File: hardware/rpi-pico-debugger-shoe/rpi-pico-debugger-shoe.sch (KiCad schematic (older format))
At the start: 2 parts, among them U1 RP2040, U2 AP2112K-3.3TRG1

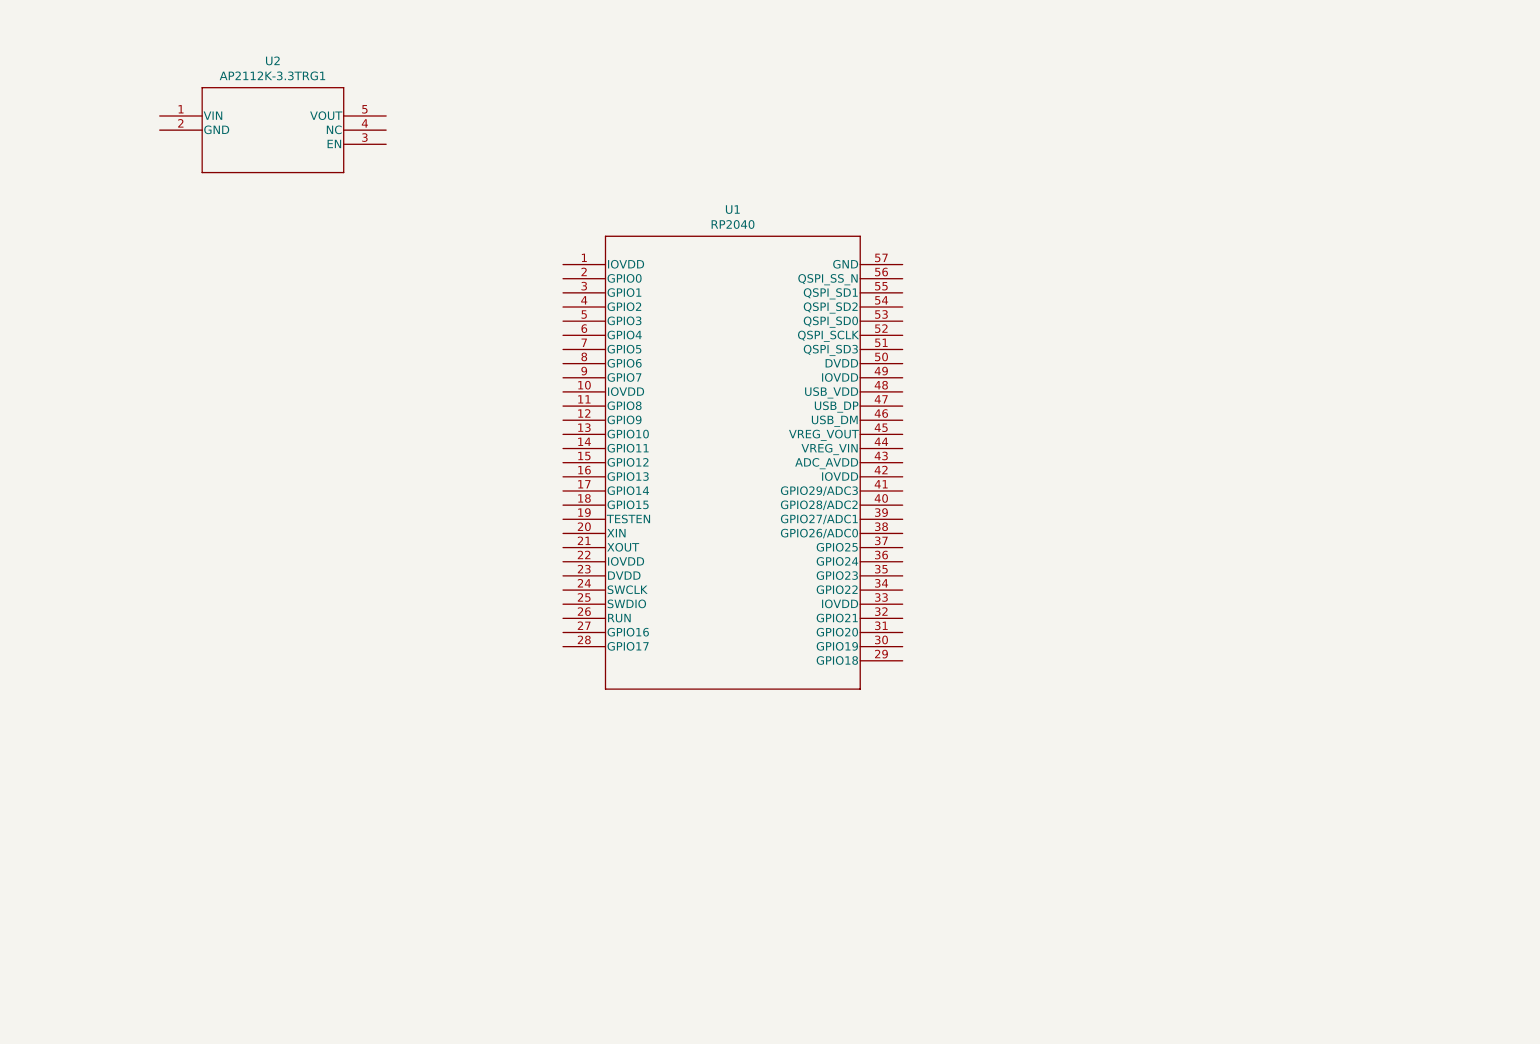
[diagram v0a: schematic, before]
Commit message: Finished schematic and BOM for v01
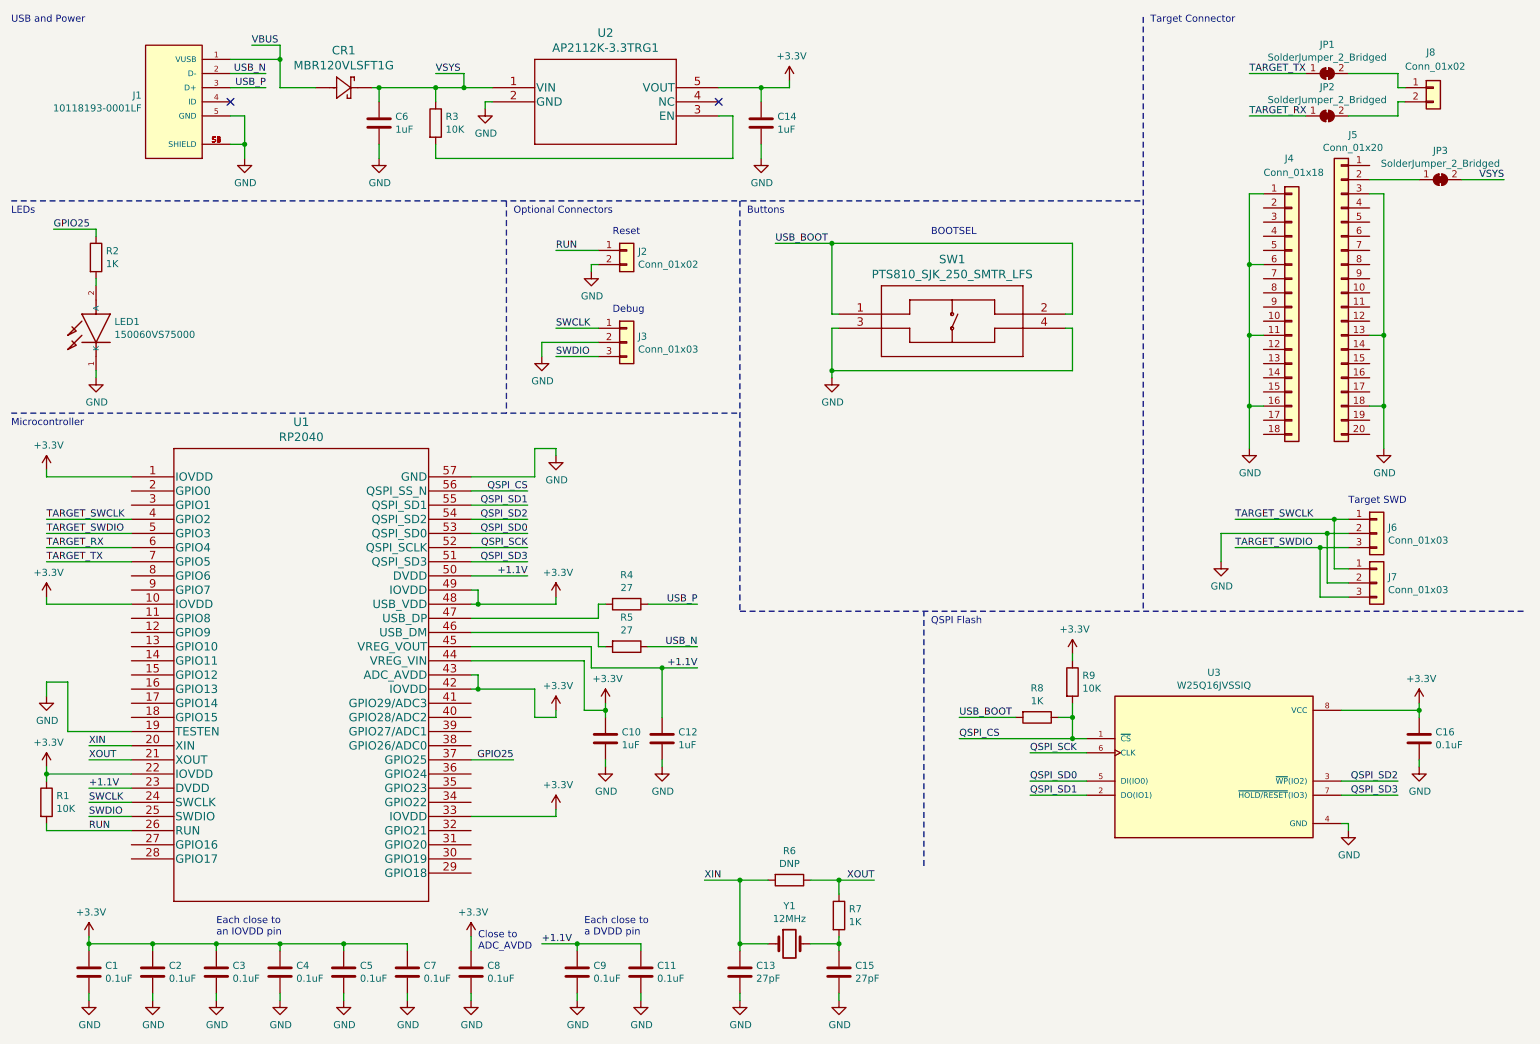
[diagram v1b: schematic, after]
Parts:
- added C1, C11, C16, C2, C3, C4, C5, C7, C8, C9: 0.1uF, Capacitor_SMD:C_0603_1608Metric_Pad1.08x0.95mm_HandSolder, symbol Device:C
- added C10, C12, C14, C6: 1uF, Capacitor_SMD:C_0603_1608Metric_Pad1.08x0.95mm_HandSolder, symbol Device:C
- added C13, C15: 27pF, Capacitor_SMD:C_0603_1608Metric_Pad1.08x0.95mm_HandSolder, symbol Device:C
- added CR1: MBR120VLSFT1G, mbr120vlsft1g:MBR120VLSFT1G, symbol 2021-05-12_00-49-18:MBR120VLSFT1G
- added J1: 10118193-0001LF, 10118193-0001LF:FCI_10118193-0001LF, symbol 10118193-0001LF:10118193-0001LF
- added J2, J8: Conn_01x02, Connector_PinHeader_2.54mm:PinHeader_1x02_P2.54mm_Vertical, symbol Connector_Generic:Conn_01x02
- added J3, J6, J7: Conn_01x03, Connector_PinHeader_2.54mm:PinHeader_1x03_P2.54mm_Vertical, symbol Connector_Generic:Conn_01x03
- added J4: Conn_01x18, Connector_PinHeader_2.54mm:PinHeader_1x18_P2.54mm_Vertical, symbol Connector_Generic:Conn_01x18
- added J5: Conn_01x20, Connector_PinHeader_2.54mm:PinHeader_1x20_P2.54mm_Vertical, symbol Connector_Generic:Conn_01x20
- added JP1, JP2, JP3: SolderJumper_2_Bridged, Jumper:SolderJumper-2_P1.3mm_Bridged_RoundedPad1.0x1.5mm, symbol Jumper:SolderJumper_2_Bridged
- added LED1: 150060VS75000, 150060VS75000:LEDC1608X80N, symbol 150060VS75000:150060VS75000
- added R1, R3, R9: 10K, Resistor_SMD:R_0603_1608Metric_Pad0.98x0.95mm_HandSolder, symbol Device:R
- added R2, R7, R8: 1K, Resistor_SMD:R_0603_1608Metric_Pad0.98x0.95mm_HandSolder, symbol Device:R
- added R4, R5: 27, Resistor_SMD:R_0603_1608Metric_Pad0.98x0.95mm_HandSolder, symbol Device:R
- added R6: DNP, Resistor_SMD:R_0603_1608Metric_Pad0.98x0.95mm_HandSolder, symbol Device:R
- added SW1: PTS810_SJK_250_SMTR_LFS, PTS810 SJK 250 SMTR LFS:PTS810 SJK 250 SMTR LFS, symbol 2021-05-12_02-12-02:PTS810_SJK_250_SMTR_LFS
- added U3: W25Q16JVSSIQ, W25Q16JVSSIQ:SOIC127P790X216-8N, symbol W25Q16JVSSIQ:W25Q16JVSSIQ
- added Y1: 12MHz, abls7m:ABLS7M2-16.000MHZ-D-2Y-T, symbol Device:Crystal
- U1: Digi-Key_PN (none) -> TBD
- U2: Digi-Key_PN (none) -> AP2112K-3.3TRG1DICT-ND
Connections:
- net +3V3: now reaches U1.1 (IOVDD)
- net +3V3: now also U1.10 (IOVDD), U1.22 (IOVDD), U1.33 (IOVDD), U1.42 (IOVDD), U1.43 (ADC_AVDD), U1.44 (VREG_VIN), U1.48 (USB_VDD), U1.49 (IOVDD), U2.5 (VOUT), C1.1, C10.1, C14.1, C16.1, C2.1, C3.1, C4.1, C5.1, C7.1, C8.1, R1.1, R9.1, U3.8 (VCC)
- net GND: now reaches U1.19 (TESTEN)
- net GND: now also U1.57 (GND), U2.2 (GND), C1.2, C10.2, C11.2, C12.2, C13.2, C14.2, C15.2, C16.2, C2.2, C3.2, C4.2, C5.2, C6.2, C7.2, C8.2, C9.2, J1.5 (GND), J1.S1 (SHIELD), J1.S2 (SHIELD), J1.S3 (SHIELD), J1.S4 (SHIELD), J1.S5 (SHIELD), J1.S6 (SHIELD), J2.2 (Pin_2), J3.2 (Pin_2), J4.1 (Pin_1), J4.11 (Pin_11), J4.16 (Pin_16), J4.6 (Pin_6), J5.13 (Pin_13), J5.18 (Pin_18), J5.3 (Pin_3), J6.2 (Pin_2), J7.2 (Pin_2), LED1.1 (K), SW1.3, SW1.4, U3.4 (GND)
- net XIN: now reaches U1.20 (XIN)
- net XIN: now also C13.1, R6.2, Y1.1
- net XOUT: now reaches U1.21 (XOUT)
- net XOUT: now also R6.1, R7.1
- net +1.1V: now reaches U1.23 (DVDD)
- net +1.1V: now also U1.45 (VREG_VOUT), U1.50 (DVDD), C11.1, C12.1, C9.1
- net SWCLK: now reaches U1.24 (SWCLK)
- net SWCLK: now also J3.1 (Pin_1)
- net SWDIO: now reaches U1.25 (SWDIO)
- net SWDIO: now also J3.3 (Pin_3)
- net RUN: now reaches U1.26 (RUN)
- net RUN: now also J2.1 (Pin_1), R1.2
- net GPIO25: now reaches U1.37 (GPIO25)
- net GPIO25: now also R2.1
- net TARGET_SWCLK: now reaches U1.4 (GPIO2)
- net TARGET_SWCLK: now also J6.1 (Pin_1), J7.1 (Pin_1)
- net at U1.46 (USB_DM): now also R5.2
- net at U1.47 (USB_DP): now also R4.2
- net TARGET_SWDIO: now reaches U1.5 (GPIO3)
- net TARGET_SWDIO: now also J6.3 (Pin_3), J7.3 (Pin_3)
- net QSPI_SD3: now reaches U1.51 (QSPI_SD3)
- net QSPI_SD3: now also U3.7 (~HOLD/RESET~(IO3))
- net QSPI_SCK: now reaches U1.52 (QSPI_SCLK)
- net QSPI_SCK: now also U3.6 (CLK)
- net QSPI_SD0: now reaches U1.53 (QSPI_SD0)
- net QSPI_SD0: now also U3.5 (DI(IO0))
- net QSPI_SD2: now reaches U1.54 (QSPI_SD2)
- net QSPI_SD2: now also U3.3 (~WP~(IO2))
- net QSPI_SD1: now reaches U1.55 (QSPI_SD1)
- net QSPI_SD1: now also U3.2 (DO(IO1))
- net QSPI_CS: now reaches U1.56 (QSPI_SS_N)
- net QSPI_CS: now also R8.1, R9.2, U3.1 (~CS)
- net TARGET_RX: now reaches U1.6 (GPIO4)
- net TARGET_RX: now also JP2.1 (A)
- net TARGET_TX: now reaches U1.7 (GPIO5)
- net TARGET_TX: now also JP1.1 (A)
- net VSYS: now reaches U2.1 (VIN)
- net VSYS: now also C6.1, CR1.1, JP3.2 (B), R3.1
- net at U2.3 (EN): now also R3.2
- new net: C15.1, R7.2, Y1.2
- new net: LED1.2 (A), R2.2
- new net: J5.2 (Pin_2), JP3.1 (A)
- new net: J8.1 (Pin_1), JP1.2 (B)
- new net: J8.2 (Pin_2), JP2.2 (B)
- new net USB_BOOT: R8.2, SW1.1, SW1.2
- new net USB_N: J1.2 (D-), R5.1
- new net USB_P: J1.3 (D+), R4.1
- new net VBUS: CR1.2, J1.1 (VUSB)
- no-connect marks 0 -> 2
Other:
- note added: "BOOTSEL"
- note added: "Buttons"
- note added: "Close to\nADC_AVDD"
- note added: "Debug"
- note added: "Each close to\na DVDD pin"
- note added: "Each close to\nan IOVDD pin"
- note added: "LEDs"
- note added: "Microcontroller"
- note added: "Optional Connectors"
- note added: "QSPI Flash"
- note added: "Reset"
- note added: "Target Connector"
- note added: "Target SWD"
- note added: "USB and Power"
- moved on the sheet: U1, U2

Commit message: Did done some layouts
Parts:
- added FID1, FID2: Fiducial, Fiducial:Fiducial_1mm_Mask2mm, symbol Mechanical:Fiducial
- added H1, H2, H3, H4: MountingHole, MountingHole:MountingHole_2.1mm, symbol Mechanical:MountingHole
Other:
- note added: "Mechanical"
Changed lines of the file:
@@
 Text Notes 7000 4800 0    50   ~ 0
 QSPI Flash
+$Comp
+L Mechanical:MountingHole H3
+U 1 1 609F6F52
+P 7800 1050
+F 0 "H3" H 7900 1096 50  0000 L CNN
+F 1 "MountingHole" H 7900 1005 50  0000 L CNN
+F 2 "MountingHole:MountingHole_2.1mm" H 7800 1050 50  0001 C CNN
+F 3 "~" H 7800 1050 50  0001 C CNN
+	1    7800 1050
+	1    0    0    -1
+$EndComp
+$Comp
+L Mechanical:MountingHole H4
+U 1 1 609F7AD6
+P 7800 1300
+F 0 "H4" H 7900 1346 50  0000 L CNN
+F 1 "MountingHole" H 7900 1255 50  0000 L CNN
+F 2 "MountingHole:MountingHole_2.1mm" H 7800 1300 50  0001 C CNN
+F 3 "~" H 7800 1300 50  0001 C CNN
+	1    7800 1300
+	1    0    0    -1
+$EndComp
+$Comp
+L Mechanical:MountingHole H2
+U 1 1 609F7D93
+P 7050 1300
+F 0 "H2" H 7150 1346 50  0000 L CNN
+F 1 "MountingHole" H 7150 1255 50  0000 L CNN
+F 2 "MountingHole:MountingHole_2.1mm" H 7050 1300 50  0001 C CNN
+F 3 "~" H 7050 1300 50  0001 C CNN
+	1    7050 1300
+	1    0    0    -1
+$EndComp
+$Comp
+L Mechanical:MountingHole H1
+U 1 1 609F81AF
+P 7050 1050
+F 0 "H1" H 7150 1096 50  0000 L CNN
+F 1 "MountingHole" H 7150 1005 50  0000 L CNN
+F 2 "MountingHole:MountingHole_2.1mm" H 7050 1050 50  0001 C CNN
+F 3 "~" H 7050 1050 50  0001 C CNN
+	1    7050 1050
+	1    0    0    -1
+$EndComp
+$Comp
+L Mechanical:Fiducial FID1
+U 1 1 609F8C47
+P 6550 1050
+F 0 "FID1" H 6635 1096 50  0000 L CNN
+F 1 "Fiducial" H 6635 1005 50  0000 L CNN
+F 2 "Fiducial:Fiducial_1mm_Mask2mm" H 6550 1050 50  0001 C CNN
+F 3 "~" H 6550 1050 50  0001 C CNN
+	1    6550 1050
+	1    0    0    -1
+$EndComp
+$Comp
+L Mechanical:Fiducial FID2
+U 1 1 609F971F
+P 6550 1300
+F 0 "FID2" H 6635 1346 50  0000 L CNN
+F 1 "Fiducial" H 6635 1255 50  0000 L CNN
+F 2 "Fiducial:Fiducial_1mm_Mask2mm" H 6550 1300 50  0001 C CNN
+F 3 "~" H 6550 1300 50  0001 C CNN
+	1    6550 1300
+	1    0    0    -1
+$EndComp
+Wire Notes Line
+	6300 500  6300 1800
+Text Notes 6350 550  0    50   ~ 0
+Mechanical
 $EndSCHEMATC

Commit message: Finished layout for v01
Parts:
- J1: footprint 10118193-0001LF:FCI_10118193-0001LF -> 10118193-0001LF:FCI_10118193-0001LF_no-slot
- J2, J8: footprint Connector_PinHeader_2.54mm:PinHeader_1x02_P2.54mm_Vertical -> custom:PinHeader_1x02_P2.54mm_Vertical_no-silk
- J3, J6, J7: footprint Connector_PinHeader_2.54mm:PinHeader_1x03_P2.54mm_Vertical -> custom:PinHeader_1x03_P2.54mm_Vertical_no-silk
- J4: footprint Connector_PinHeader_2.54mm:PinHeader_1x18_P2.54mm_Vertical -> custom:PinHeader_1x18_P2.54mm_Vertical_no-silk
- J5: footprint Connector_PinHeader_2.54mm:PinHeader_1x20_P2.54mm_Vertical -> custom:PinHeader_1x20_P2.54mm_Vertical_no-silk
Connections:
- net GND: now also J5.8 (Pin_8)
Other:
- note added: "Cut to provide\nseparate power\nto target Pico"
- note removed: "Mechanical"
- moved on the sheet: FID1, FID2, H1, H2, H3, H4
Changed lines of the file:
@@
 F 0 "J1" H 1878 1146 50  0000 L CNN
 F 1 "10118193-0001LF" H 1878 1055 50  0000 L CNN
-F 2 "10118193-0001LF:FCI_10118193-0001LF" H 1650 1100 50  0001 L BNN
+F 2 "10118193-0001LF:FCI_10118193-0001LF_no-slot" H 1650 1100 50  0001 L BNN
 F 3 "" H 1650 1100 50  0001 L BNN
 F 4 "Single Port 5 Contact Shielded SMT MICRO USB B-Type Receptacle" H 1650 1100 50  0001 L BNN "DESCRIPTION"
@@
 F 0 "J3" H 4930 2842 50  0000 L CNN
 F 1 "Conn_01x03" H 4930 2751 50  0000 L CNN
-F 2 "Connector_PinHeader_2.54mm:PinHeader_1x03_P2.54mm_Vertical" H 4850 2800 50  0001 C CNN
+F 2 "custom:PinHeader_1x03_P2.54mm_Vertical_no-silk" H 4850 2800 50  0001 C CNN
 F 3 "~" H 4850 2800 50  0001 C CNN
 	1    4850 2800
@@
 F 0 "J2" H 4930 2142 50  0000 L CNN
 F 1 "Conn_01x02" H 4930 2051 50  0000 L CNN
-F 2 "Connector_PinHeader_2.54mm:PinHeader_1x02_P2.54mm_Vertical" H 4850 2150 50  0001 C CNN
+F 2 "custom:PinHeader_1x02_P2.54mm_Vertical_no-silk" H 4850 2150 50  0001 C CNN
 F 3 "~" H 4850 2150 50  0001 C CNN
 	1    4850 2150
@@
 F 0 "J4" H 9500 3600 50  0000 L CNN
 F 1 "Conn_01x18" H 9350 3500 50  0000 L CNN
-F 2 "Connector_PinHeader_2.54mm:PinHeader_1x18_P2.54mm_Vertical" H 9550 2550 50  0001 C CNN
+F 2 "custom:PinHeader_1x18_P2.54mm_Vertical_no-silk" H 9550 2550 50  0001 C CNN
 F 3 "~" H 9550 2550 50  0001 C CNN
 F 4 "1988-1035-ND" H 9550 2550 50  0001 C CNN "Digi-Key_PN"
@@
 F 0 "J5" H 9818 3567 50  0000 C CNN
 F 1 "Conn_01x20" H 9818 3476 50  0000 C CNN
-F 2 "Connector_PinHeader_2.54mm:PinHeader_1x20_P2.54mm_Vertical" H 9900 2450 50  0001 C CNN
+F 2 "custom:PinHeader_1x20_P2.54mm_Vertical_no-silk" H 9900 2450 50  0001 C CNN
 F 3 "~" H 9900 2450 50  0001 C CNN
 F 4 "1988-1136-ND" H 9900 2450 50  0001 C CNN "Digi-Key_PN"
@@
 F 0 "J8" H 10500 1250 50  0000 L CNN
 F 1 "Conn_01x02" H 10350 1150 50  0000 L CNN
-F 2 "Connector_PinHeader_2.54mm:PinHeader_1x02_P2.54mm_Vertical" H 10550 1000 50  0001 C CNN
+F 2 "custom:PinHeader_1x02_P2.54mm_Vertical_no-silk" H 10550 1000 50  0001 C CNN
 F 3 "~" H 10550 1000 50  0001 C CNN
 F 4 "S7035-ND" H 10550 1000 50  0001 C CNN "Digi-Key_PN"
@@
 F 0 "J6" H 10230 4192 50  0000 L CNN
 F 1 "Conn_01x03" H 10230 4101 50  0000 L CNN
-F 2 "Connector_PinHeader_2.54mm:PinHeader_1x03_P2.54mm_Vertical" H 10150 4150 50  0001 C CNN
+F 2 "custom:PinHeader_1x03_P2.54mm_Vertical_no-silk" H 10150 4150 50  0001 C CNN
 F 3 "~" H 10150 4150 50  0001 C CNN
 	1    10150 4150
@@
 	10100 1750 10200 1750
 Wire Wire Line
-	10200 1750 10200 2750
+	10200 1750 10200 2250
 Wire Wire Line
 	10100 3250 10200 3250
@@
 F 0 "J7" H 10230 4542 50  0000 L CNN
 F 1 "Conn_01x03" H 10230 4451 50  0000 L CNN
-F 2 "Connector_PinHeader_2.54mm:PinHeader_1x03_P2.54mm_Vertical" H 10150 4500 50  0001 C CNN
+F 2 "custom:PinHeader_1x03_P2.54mm_Vertical_no-silk" H 10150 4500 50  0001 C CNN
 F 3 "~" H 10150 4500 50  0001 C CNN
 F 4 "S7036-ND" H 10150 4500 50  0001 C CNN "Digi-Key_PN"
@@
 L Mechanical:MountingHole H3
 U 1 1 609F6F52
-P 7800 1050
-F 0 "H3" H 7900 1096 50  0000 L CNN
-F 1 "MountingHole" H 7900 1005 50  0000 L CNN
-F 2 "MountingHole:MountingHole_2.1mm" H 7800 1050 50  0001 C CNN
-F 3 "~" H 7800 1050 50  0001 C CNN
-	1    7800 1050
+P 11000 6700
+F 0 "H3" H 11100 6746 50  0000 L CNN
+F 1 "MountingHole" H 11100 6655 50  0001 L CNN
+F 2 "MountingHole:MountingHole_2.1mm" H 11000 6700 50  0001 C CNN
+F 3 "~" H 11000 6700 50  0001 C CNN
+	1    11000 6700
 	1    0    0    -1
 $EndComp
@@
 L Mechanical:MountingHole H4
 U 1 1 609F7AD6
-P 7800 1300
-F 0 "H4" H 7900 1346 50  0000 L CNN
-F 1 "MountingHole" H 7900 1255 50  0000 L CNN
-F 2 "MountingHole:MountingHole_2.1mm" H 7800 1300 50  0001 C CNN
-F 3 "~" H 7800 1300 50  0001 C CNN
-	1    7800 1300
+P 11000 6950
+F 0 "H4" H 11100 6996 50  0000 L CNN
+F 1 "MountingHole" H 11100 6905 50  0001 L CNN
+F 2 "MountingHole:MountingHole_2.1mm" H 11000 6950 50  0001 C CNN
+F 3 "~" H 11000 6950 50  0001 C CNN
+	1    11000 6950
 	1    0    0    -1
 $EndComp
@@
 L Mechanical:MountingHole H2
 U 1 1 609F7D93
-P 7050 1300
-F 0 "H2" H 7150 1346 50  0000 L CNN
-F 1 "MountingHole" H 7150 1255 50  0000 L CNN
-F 2 "MountingHole:MountingHole_2.1mm" H 7050 1300 50  0001 C CNN
-F 3 "~" H 7050 1300 50  0001 C CNN
-	1    7050 1300
+P 10700 6950
+F 0 "H2" H 10800 6996 50  0000 L CNN
+F 1 "MountingHole" H 10800 6905 50  0001 L CNN
+F 2 "MountingHole:MountingHole_2.1mm" H 10700 6950 50  0001 C CNN
+F 3 "~" H 10700 6950 50  0001 C CNN
+	1    10700 6950
 	1    0    0    -1
 $EndComp
@@
 L Mechanical:MountingHole H1
 U 1 1 609F81AF
-P 7050 1050
-F 0 "H1" H 7150 1096 50  0000 L CNN
-F 1 "MountingHole" H 7150 1005 50  0000 L CNN
-F 2 "MountingHole:MountingHole_2.1mm" H 7050 1050 50  0001 C CNN
-F 3 "~" H 7050 1050 50  0001 C CNN
-	1    7050 1050
+P 10700 6700
+F 0 "H1" H 10800 6746 50  0000 L CNN
+F 1 "MountingHole" H 10800 6655 50  0001 L CNN
+F 2 "MountingHole:MountingHole_2.1mm" H 10700 6700 50  0001 C CNN
+F 3 "~" H 10700 6700 50  0001 C CNN
+	1    10700 6700
 	1    0    0    -1
 $EndComp
@@
 L Mechanical:Fiducial FID1
 U 1 1 609F8C47
-P 6550 1050
-F 0 "FID1" H 6635 1096 50  0000 L CNN
-F 1 "Fiducial" H 6635 1005 50  0000 L CNN
-F 2 "Fiducial:Fiducial_1mm_Mask2mm" H 6550 1050 50  0001 C CNN
-F 3 "~" H 6550 1050 50  0001 C CNN
-	1    6550 1050
+P 10350 6700
+F 0 "FID1" H 10435 6746 50  0000 L CNN
+F 1 "Fiducial" H 10435 6655 50  0001 L CNN
+F 2 "Fiducial:Fiducial_1mm_Mask2mm" H 10350 6700 50  0001 C CNN
+F 3 "~" H 10350 6700 50  0001 C CNN
+	1    10350 6700
 	1    0    0    -1
 $EndComp
@@
 L Mechanical:Fiducial FID2
 U 1 1 609F971F
-P 6550 1300
-F 0 "FID2" H 6635 1346 50  0000 L CNN
-F 1 "Fiducial" H 6635 1255 50  0000 L CNN
-F 2 "Fiducial:Fiducial_1mm_Mask2mm" H 6550 1300 50  0001 C CNN
-F 3 "~" H 6550 1300 50  0001 C CNN
-	1    6550 1300
-	1    0    0    -1
-$EndComp
-Wire Notes Line
-	6300 500  6300 1800
-Text Notes 6350 550  0    50   ~ 0
-Mechanical
+P 10350 6950
+F 0 "FID2" H 10435 6996 50  0000 L CNN
+F 1 "Fiducial" H 10435 6905 50  0001 L CNN
+F 2 "Fiducial:Fiducial_1mm_Mask2mm" H 10350 6950 50  0001 C CNN
+F 3 "~" H 10350 6950 50  0001 C CNN
+	1    10350 6950
+	1    0    0    -1
+$EndComp
+Text Notes 10350 2000 0    50   ~ 0
+Cut to provide\nseparate power\nto target Pico
+Wire Wire Line
+	10100 2250 10200 2250
+Connection ~ 10200 2250
+Wire Wire Line
+	10200 2250 10200 2750
 $EndSCHEMATC
